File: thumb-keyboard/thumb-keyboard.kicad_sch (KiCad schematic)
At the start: 124 parts, among them J1 Conn_01x02_Socket, U1 nice_nano

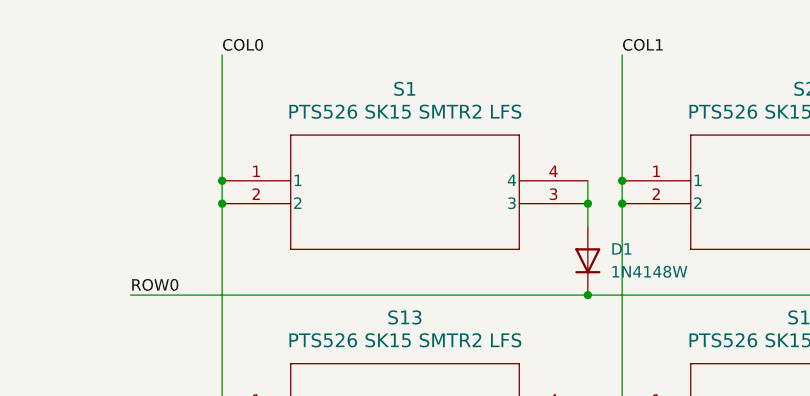
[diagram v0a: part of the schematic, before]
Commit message: going to try reducing the slot diam
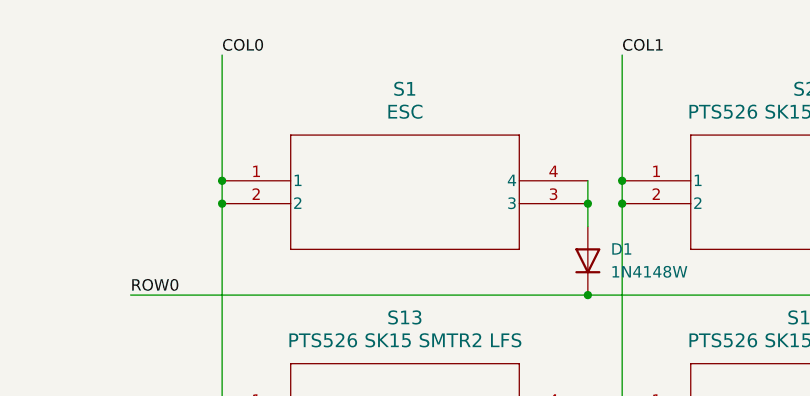
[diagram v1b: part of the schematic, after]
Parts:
- S1: value PTS526 SK15 SMTR2 LFS -> ESC
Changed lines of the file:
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@@
 			)
 		)
-		(property "Value" "PTS526 SK15 SMTR2 LFS"
+		(property "Value" "ESC"
 			(at 129.54 38.1 0)
 			(effects

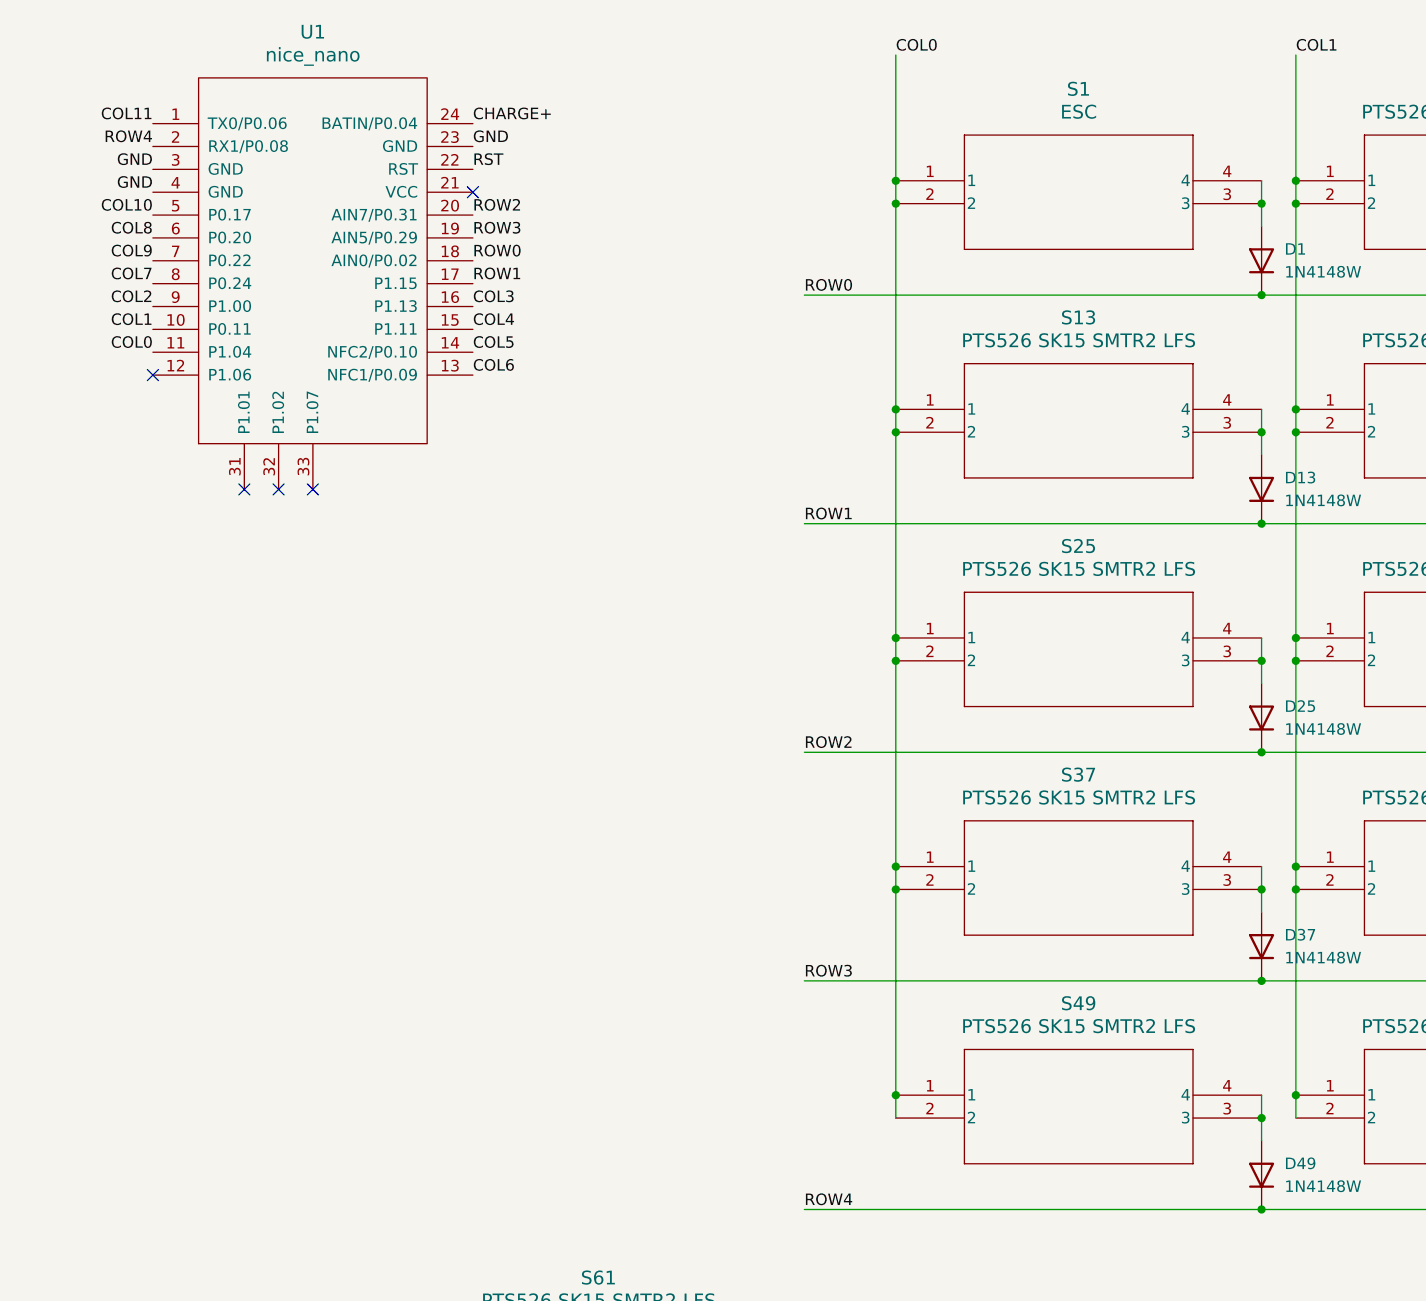
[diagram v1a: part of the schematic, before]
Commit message: Added ws2812b leds to thumb keyboard. they may be too tall. I may have to switch to the 222AMVBAR tactile switches and space everything out like a centimeter more. that would be a lot of work but would open up for other types of switches
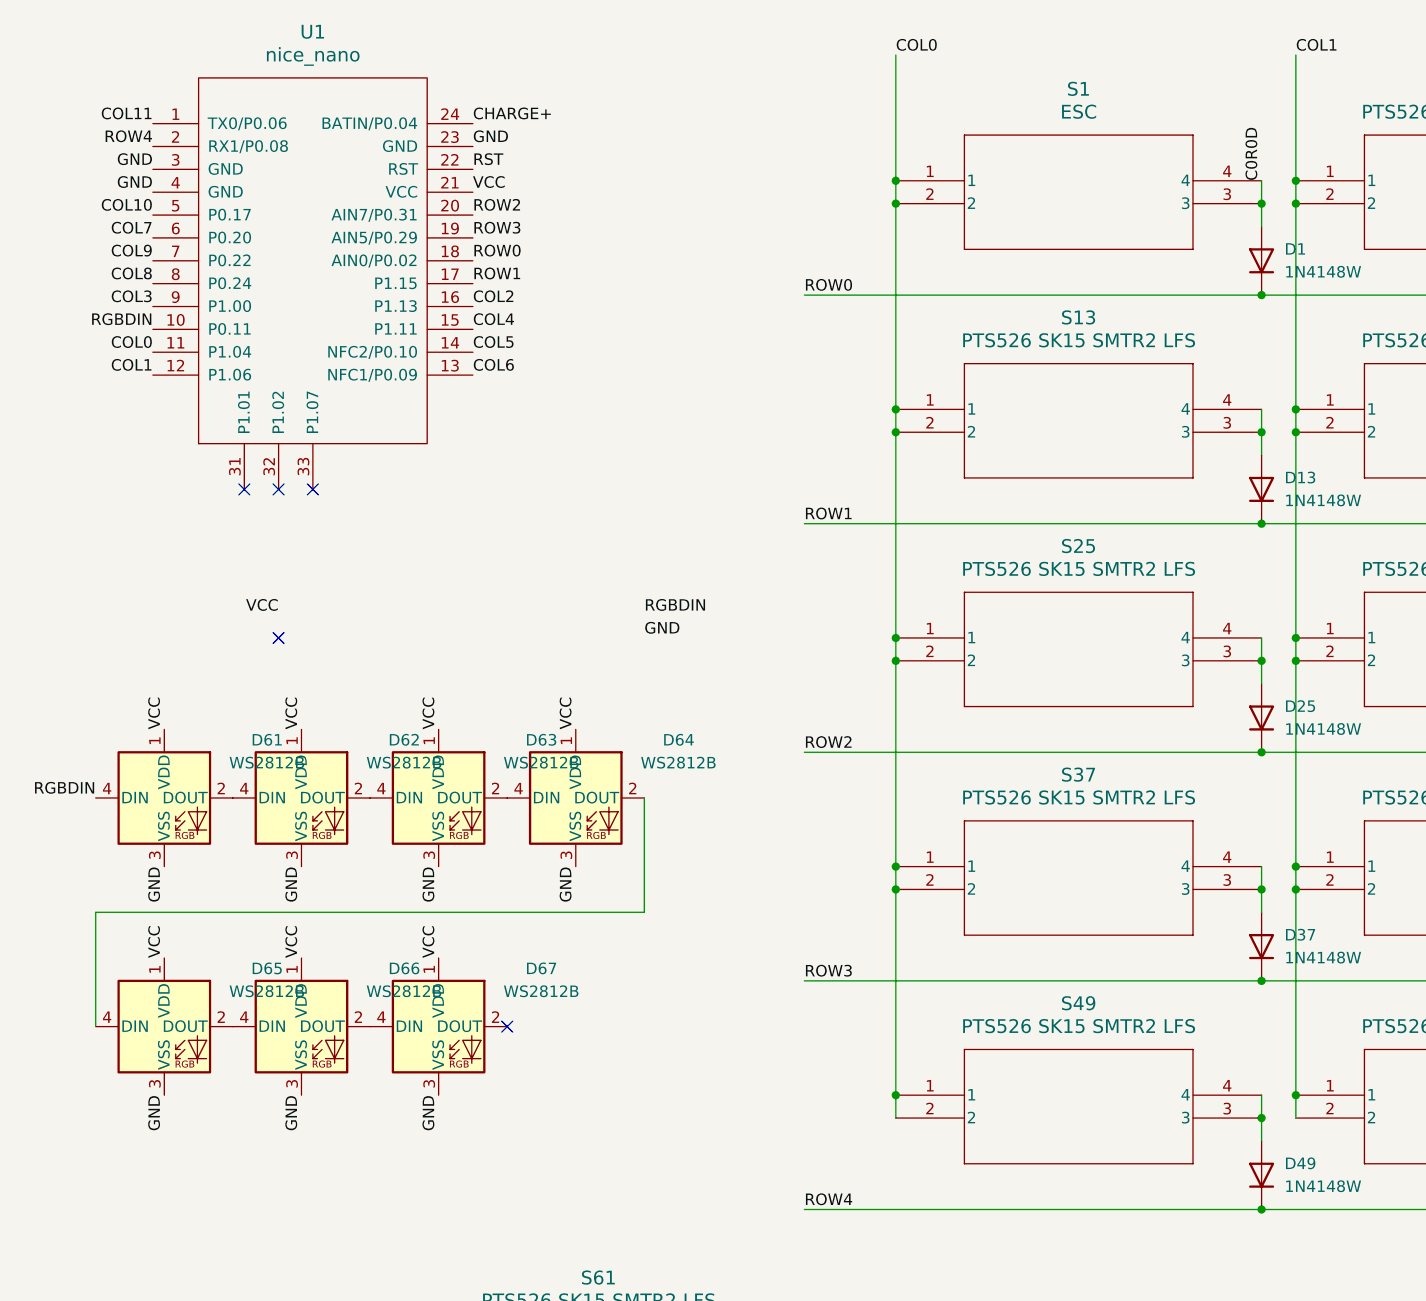
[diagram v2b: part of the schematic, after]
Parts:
- added D61, D62, D63, D64, D65, D66, D67: WS2812B, LED_SMD:LED_WS2812B_PLCC4_5.0x5.0mm_P3.2mm, symbol LED:WS2812B
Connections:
- net COL1: now also U1.12 (P1.06); no longer U1.10 (P0.11)
- net COL2: now also U1.16 (P1.13); no longer U1.9 (P1.00)
- net COL3: now also U1.9 (P1.00); no longer U1.16 (P1.13)
- net COL7: now also U1.6 (P0.20); no longer U1.8 (P0.24)
- net COL8: now also U1.8 (P0.24); no longer U1.6 (P0.20)
- net GND: now also D61.3 (VSS), D62.3 (VSS), D63.3 (VSS), D64.3 (VSS), D65.3 (VSS), D66.3 (VSS), D67.3 (VSS)
- net VCC: now reaches U1.21 (VCC)
- net VCC: now also D61.1 (VDD), D62.1 (VDD), D63.1 (VDD), D64.1 (VDD), D65.1 (VDD), D66.1 (VDD), D67.1 (VDD)
- net C0R0D: now reaches D1.2 (A), S1.3, S1.4
- new net: D65.2 (DOUT), D66.4 (DIN)
- new net: D64.2 (DOUT), D65.4 (DIN)
- new net: D66.2 (DOUT), D67.4 (DIN)
- new net: D63.2 (DOUT), D64.4 (DIN)
- new net: D62.2 (DOUT), D63.4 (DIN)
- new net: D61.2 (DOUT), D62.4 (DIN)
- new net RGBDIN: D61.4 (DIN), U1.10 (P0.11)

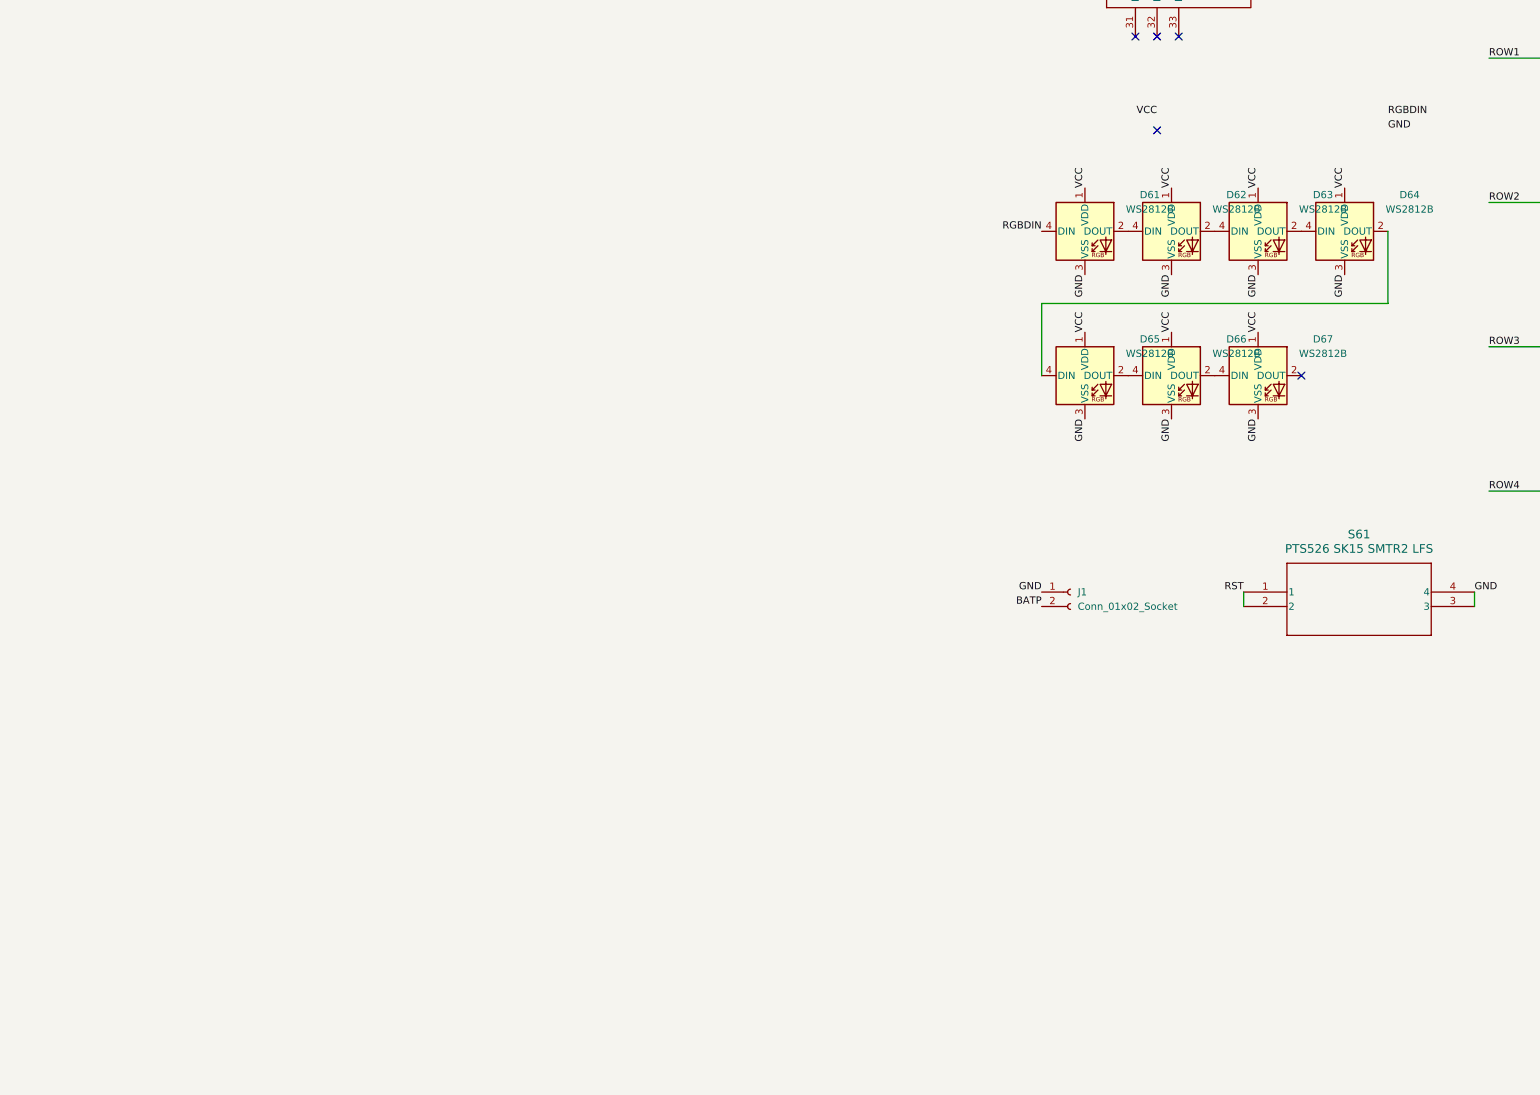
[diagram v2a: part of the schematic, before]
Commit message: working on different switches. last commit before adding the B3F-1000 switch option and extending the x gap from 10 - 12 mm
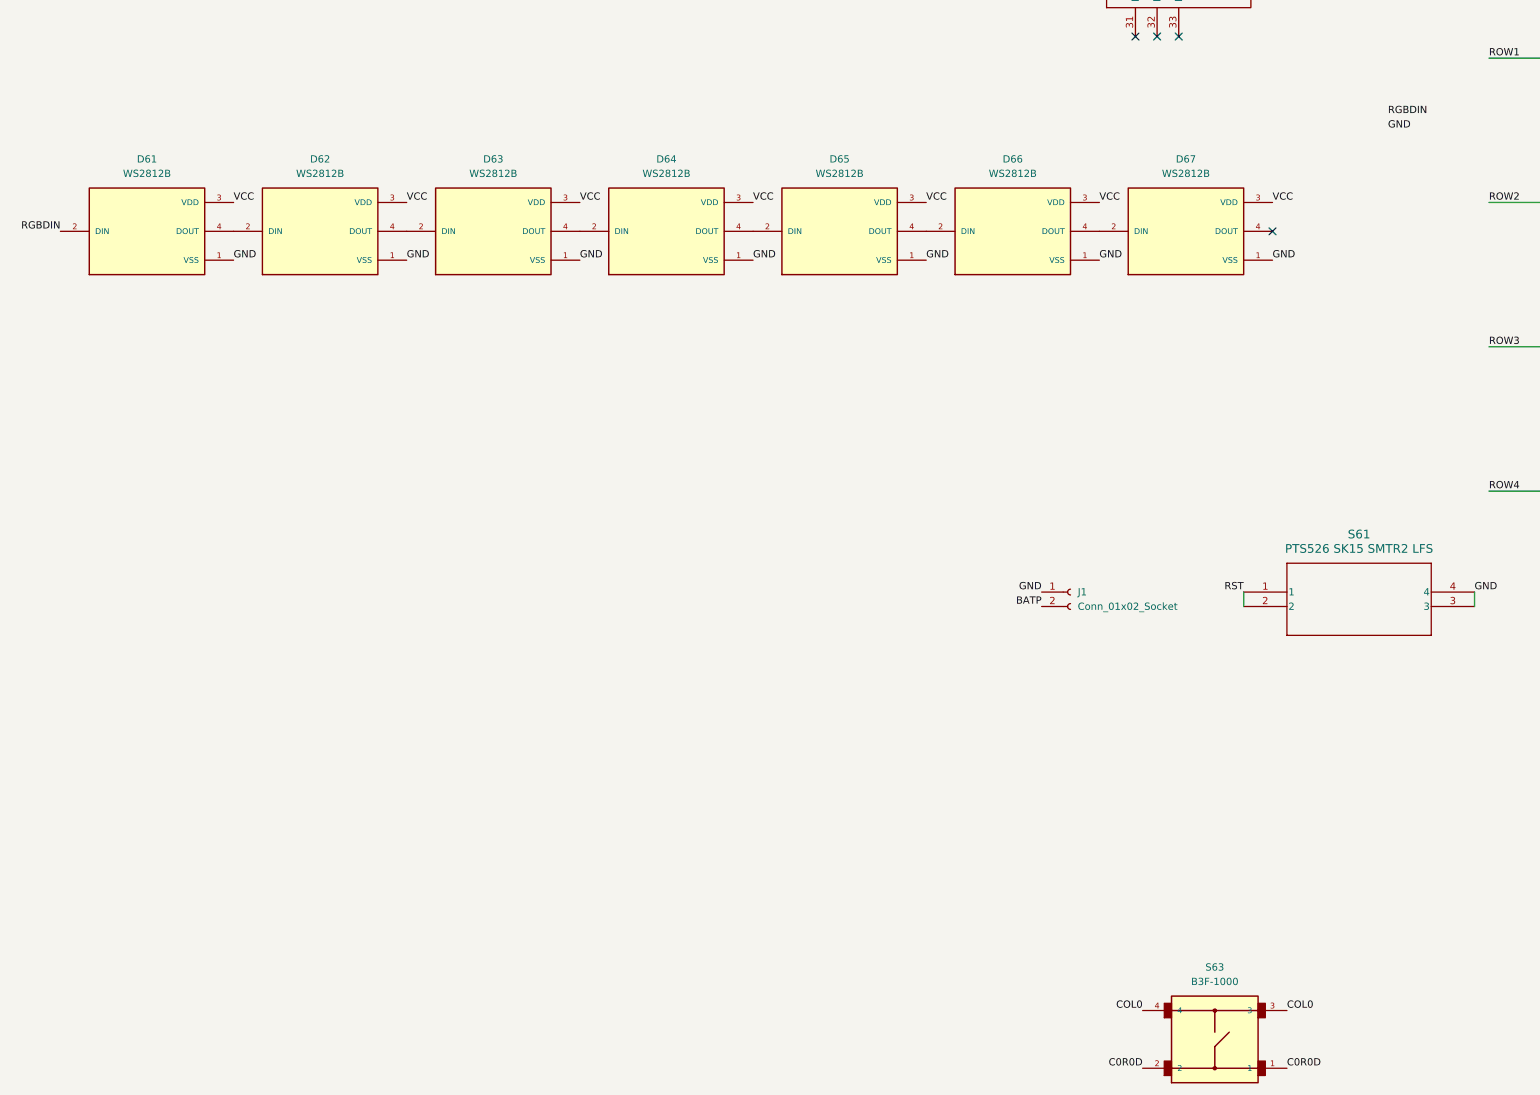
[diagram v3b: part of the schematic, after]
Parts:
- added S63: B3F-1000, B3F_1000:SW_B3F-1000, symbol B3F-1000:B3F-1000
- D61, D62, D63, D64, D65, D66, D67: footprint LED_SMD:LED_WS2812B_PLCC4_5.0x5.0mm_P3.2mm -> 1655:LED_1655; symbol LED:WS2812B -> 1655:1655; MANUFACTURER (none) -> Adafruit Industries; MAXIMUM_PACKAGE_HEIGHT (none) -> 1.6 mm; PARTREV (none) -> 01; STANDARD (none) -> Manufacturer recommendations
- S1, S10, S11, S12, S13, S14, S15, S16, S17, S18, S19, S2, S20, S21, S22, S23, S24, S25, S26, S27, S28, S29, S3, S30, S31, S32, S33, S34, S35, S36, S37, S38, S39, S4, S40, S41, S42, S43, S44, S45, S46, S47, S48, S49, S5, S50, S51, S52, S53, S54, S55, S56, S57, S58, S59, S6, S60, S61, S7, S8, S9: footprint SMT_FS -> lowproswitch:SMT_FS
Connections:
- net C0R0D: now also S63.1, S63.2
- net COL0: now also S63.3, S63.4
- net GND: now also D61.1 (VSS), D62.1 (VSS), D63.1 (VSS), D64.1 (VSS), D65.1 (VSS), D66.1 (VSS), D67.1 (VSS); no longer D61.3 (VSS), D62.3 (VSS), D63.3 (VSS), D64.3 (VSS), D65.3 (VSS), D66.3 (VSS), D67.3 (VSS)
- net RGBDIN: now also D61.2 (DIN); no longer D61.4 (DIN)
- net VCC: now also D61.3 (VDD), D62.3 (VDD), D63.3 (VDD), D64.3 (VDD), D65.3 (VDD), D66.3 (VDD), D67.3 (VDD); no longer D61.1 (VDD), D62.1 (VDD), D63.1 (VDD), D64.1 (VDD), D65.1 (VDD), D66.1 (VDD), D67.1 (VDD)
- net at D65.2 (DIN): now also D64.4 (DOUT); no longer D66.4 (DIN)
- net at D65.4 (DOUT): now also D66.2 (DIN); no longer D64.2 (DOUT)
- net at D67.2 (DIN): now also D66.4 (DOUT)
- net at D67.4 (DOUT): no longer D66.2 (DOUT)
- net at D63.2 (DIN): now also D62.4 (DOUT); no longer D64.4 (DIN)
- net at D63.4 (DOUT): now also D64.2 (DIN); no longer D62.2 (DOUT)
- new net: D61.4 (DOUT), D62.2 (DIN)
- no-connect marks 6 -> 5
